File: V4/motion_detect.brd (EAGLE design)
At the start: 42.1 x 50 mm, 54 parts, among them CON2 PINHEAD_1X01-2.54, IC1 AM612, IC2 AM312, IC3 3.3, IC4 ATMEGA168-TQFP32, Q1 IRLML2244TRPBF, Q6 IRLML2502-SOT23, Q7 IRLML2244TRPBF, SW1 TACT_SWITCH-IT-1102S

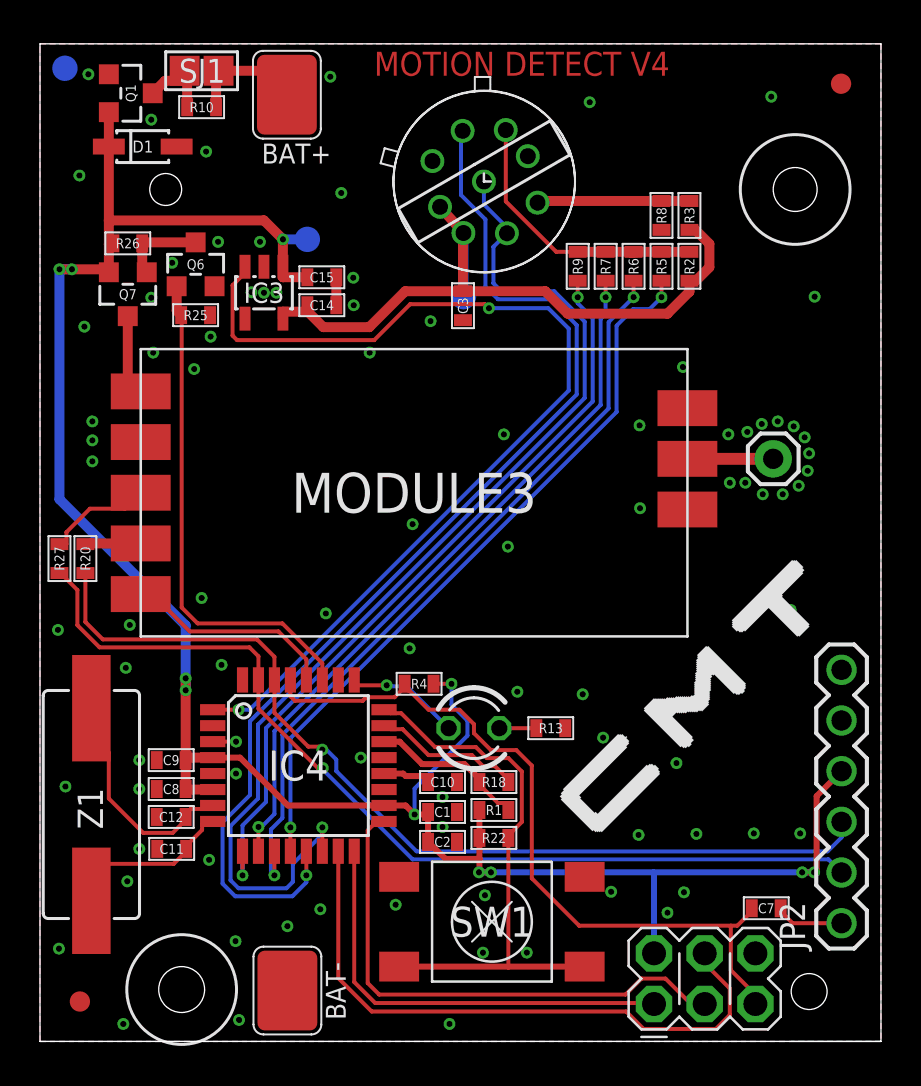
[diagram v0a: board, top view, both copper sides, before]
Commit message: vias update
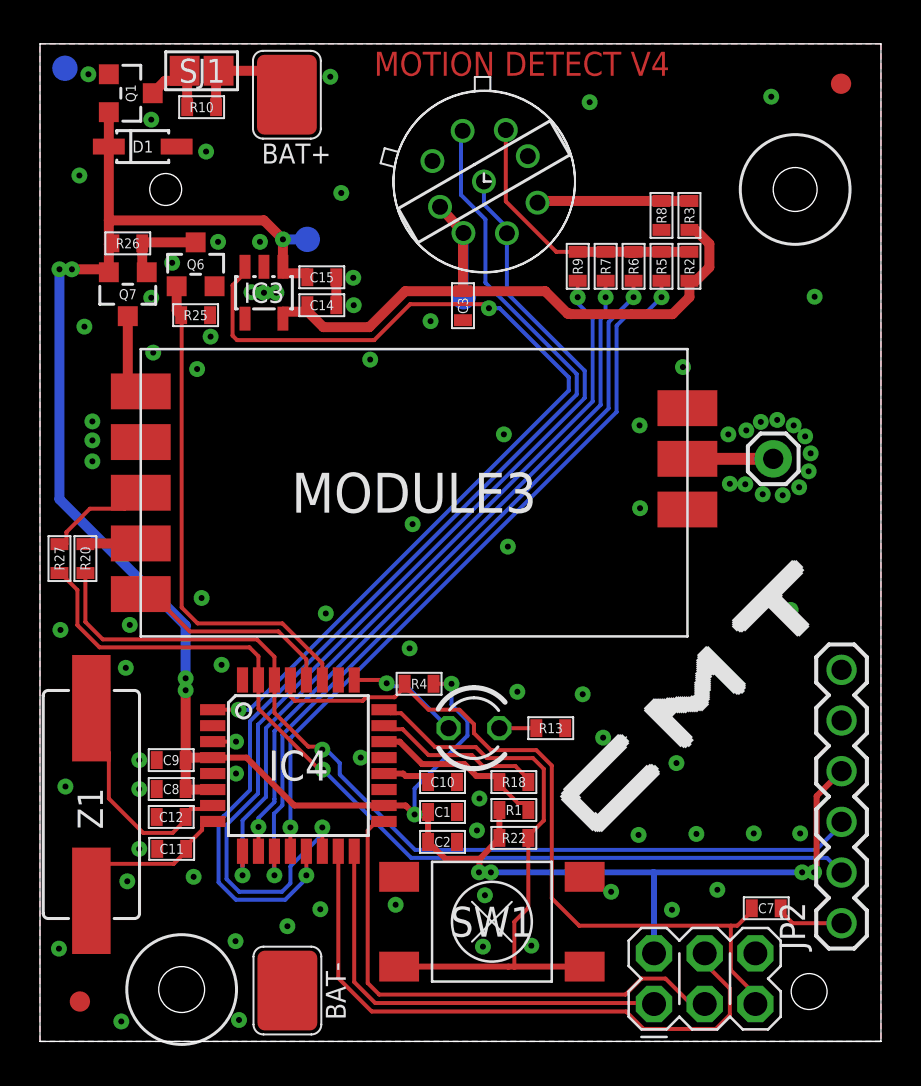
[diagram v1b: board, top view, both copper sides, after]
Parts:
- moved R1 1.00 mm to (23.8, 11.6)
- moved R18 1.00 mm to (23.8, 13.0)
- moved R22 1.00 mm to (23.8, 10.2)
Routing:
- net D10: track 54.5 -> 52.8 mm
- net A1: track 28.0 -> 29.5 mm
- net D3: track 49.5 -> 48.0 mm
- net D9: track 55.4 -> 54.2 mm
- net A0: track 7.48 -> 8.49 mm
- net ADC7: track 7.90 -> 8.90 mm
- net RST: track 37.9 -> 38.5 mm
- net GND: vias 87 -> 86

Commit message: Production files added
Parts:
- R5: value val3 -> 330K
- R6: value val2 -> 330K
- R7: value val1 -> 330K
- R9: value val1 -> 000
- renumbered LED5 to LED1
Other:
- board text added: "IC1"
